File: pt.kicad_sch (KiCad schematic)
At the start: 5 parts, among them J18 PT

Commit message: Updated schematic. No filtering but besides that finished. Need to fix footprints and start layout.
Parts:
- J18: footprint TerminalBlock:TerminalBlock_bornier-3_P5.08mm -> 0UCIRP-KiCAD-Lib:GX-12 3 pin

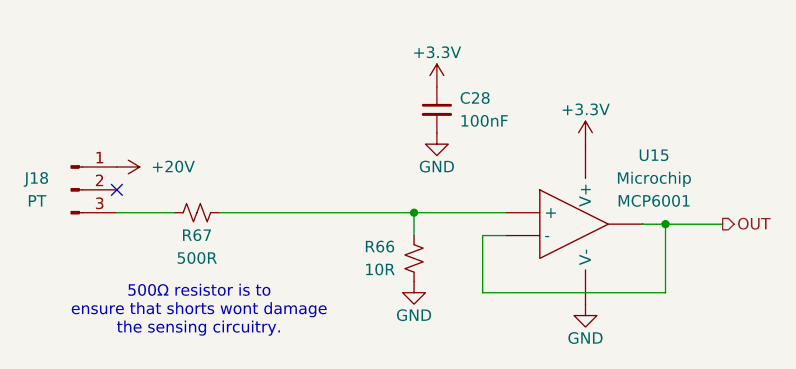
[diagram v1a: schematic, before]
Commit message: Added LC filter for power filtering
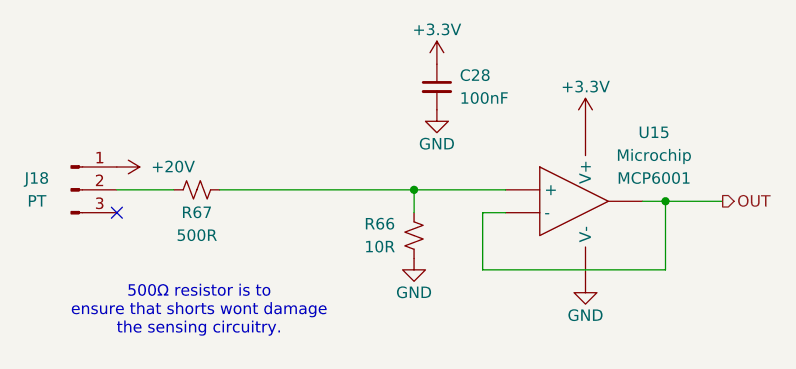
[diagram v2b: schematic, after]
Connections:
- net at J18.2 (Pin_2): now also R67.2
- net at J18.3 (Pin_3): no longer R67.2
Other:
- moved on the sheet: C28, R66, R67, U15

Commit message: Updates after PDR
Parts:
- added C69: ?, Capacitor_SMD:C_0402_1005Metric, symbol Device:C_Small
- added C87: 100nF, Capacitor_SMD:C_0402_1005Metric, symbol Device:C_Small
- added D26: BZT52H, Diode_SMD:D_SOD-123F, symbol UCIRP-KiCAD-Lib:D_Zener_Small
- added R7: 0R, Resistor_SMD:R_0402_1005Metric, symbol Device:R_Small_US
- added U39: ~, Package_TO_SOT_SMD:SOT-23-5, symbol UCIRP-KiCAD-Lib:MCP6001
- R66: value 10R -> 500R
- U15: Manufacturer Microchip -> Texas Instruments; Part # MCP6001 -> LMC7101
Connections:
- net GND: now also C69.2, C87.2, D26.2 (A), U39.2 (V-)
- net OUT: now also U39.1, U39.4 (-); no longer U15.1, U15.4 (-)
- net at R66.2, R67.1, U15.3 (+): now also D26.1 (K)
- net +3.3V renamed +10V
- net +10V: now also C87.1, U39.5 (V+)
- new net: R7.2, U15.1, U15.4 (-)
- new net: C69.1, R7.1, U39.3 (+)
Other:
- note added: "Configurable low pass filter"
- note added: "Zener diode caps voltage at 10V"
- note removed: "500Ω resistor is to ensure that shorts wont damage the sensing circuitry."
- moved on the sheet: R66

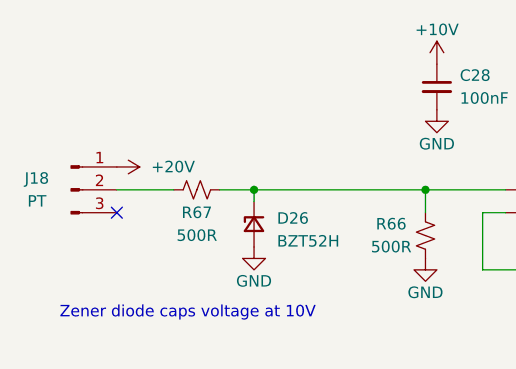
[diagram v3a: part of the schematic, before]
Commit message: Updated to add beginnings of layout. Most major subsystems internally layed out
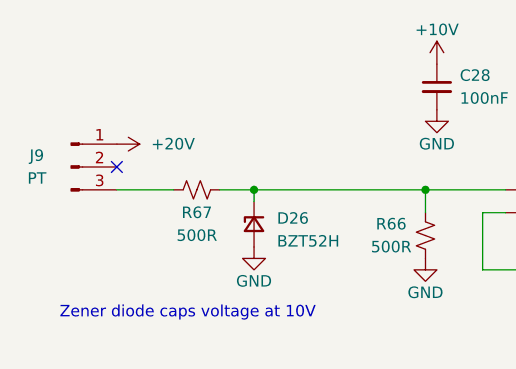
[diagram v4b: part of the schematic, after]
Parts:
- removed J18: PT, 0UCIRP-KiCAD-Lib:GX-12 3 pin, symbol Connector:Conn_01x03_Pin
- added J9: PT, 0UCIRP-KiCAD-Lib:GX-12 3 pin, symbol Connector:Conn_01x03_Pin
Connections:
- net +20V: now also J9.1 (Pin_1)
- net at R67.2: now also J9.3 (Pin_3)
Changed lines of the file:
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@@
 	)
 	(no_connect
-		(at 109.22 96.52)
+		(at 109.22 91.44)
 	)
 	(wire
@@
 	(symbol
 		(lib_id "power:+24V")
-		(at 109.22 91.44 270)
+		(at 109.22 88.9 270)
 		(unit 1)
 		(exclude_from_sim no)
@@
 		(fields_autoplaced yes)
 		(property "Reference" "#PWR0167"
-			(at 105.41 91.44 0)
+			(at 105.41 88.9 0)
 			(effects
 				(font
@@
 		)
 		(property "Value" "+20V"
-			(at 113.03 91.44 90)
+			(at 113.03 88.9 90)
 			(effects
 				(font
@@
 		)
 		(property "Footprint" ""
-			(at 109.22 91.44 0)
+			(at 109.22 88.9 0)
 			(effects
 				(font
@@
 		)
 		(property "Datasheet" ""
-			(at 109.22 91.44 0)
+			(at 109.22 88.9 0)
 			(effects
 				(font
@@
 		)
 		(property "Description" ""
-			(at 109.22 91.44 0)
+			(at 109.22 88.9 0)
 			(effects
 				(font
@@
 	)
 	(symbol
-		(lib_id "Connector:Conn_01x03_Pin")
-		(at 104.14 93.98 0)
-		(unit 1)
-		(exclude_from_sim no)
-		(in_bom yes)
-		(on_board yes)
-		(dnp no)
-		(property "Reference" "J18"
-			(at 100.33 92.71 0)
-			(effects
-				(font
-					(size 1.27 1.27)
-				)
-			)
-		)
-		(property "Value" "PT"
-			(at 100.33 95.25 0)
-			(effects
-				(font
-					(size 1.27 1.27)
-				)
-			)
-		)
-		(property "Footprint" "0UCIRP-KiCAD-Lib:GX-12 3 pin"
-			(at 104.14 93.98 0)
-			(effects
-				(font
-					(size 1.27 1.27)
-				)
-				(hide yes)
-			)
-		)
-		(property "Datasheet" "~"
-			(at 104.14 93.98 0)
-			(effects
-				(font
-					(size 1.27 1.27)
-				)
-				(hide yes)
-			)
-		)
-		(property "Description" ""
-			(at 104.14 93.98 0)
-			(effects
-				(font
-					(size 1.27 1.27)
-				)
-			)
-		)
-		(property "Manufacturer" "~"
-			(at 104.14 93.98 0)
-			(effects
-				(font
-					(size 1.27 1.27)
-				)
-				(hide yes)
-			)
-		)
-		(property "Part #" "~"
-			(at 104.14 93.98 0)
-			(effects
-				(font
-					(size 1.27 1.27)
-				)
-				(hide yes)
-			)
-		)
-		(pin "1"
-		)
-		(pin "2"
-		)
-		(pin "3"
-		)
-		(instances
-			(project "gse2-hardware"
-				(path "/1eb2a3ff-e0fd-4343-8dba-716780a4d459/080ef17d-44b6-48a5-becc-c956f0d3b11f"
-					(reference "J26")
-					(unit 1)
-				)
-				(path "/1eb2a3ff-e0fd-4343-8dba-716780a4d459/0c63aa72-2f8c-4349-a8c7-c0452c52d596"
-					(reference "J18")
-					(unit 1)
-				)
-				(path "/1eb2a3ff-e0fd-4343-8dba-716780a4d459/3a1ca63f-f82f-4b0b-969f-686d8e871d34"
-					(reference "J20")
-					(unit 1)
-				)
-				(path "/1eb2a3ff-e0fd-4343-8dba-716780a4d459/7562866f-379c-4e40-8214-10fa496db888"
-					(reference "J28")
-					(unit 1)
-				)
-				(path "/1eb2a3ff-e0fd-4343-8dba-716780a4d459/90511ce4-e980-4cde-b5eb-16766304f657"
-					(reference "J22")
-					(unit 1)
-				)
-				(path "/1eb2a3ff-e0fd-4343-8dba-716780a4d459/964f4378-b8db-4e43-9e59-375ac742ee34"
-					(reference "J19")
-					(unit 1)
-				)
-				(path "/1eb2a3ff-e0fd-4343-8dba-716780a4d459/b677298a-c5d8-49cc-b7d8-b72cad589e13"
-					(reference "J29")
-					(unit 1)
-				)
-				(path "/1eb2a3ff-e0fd-4343-8dba-716780a4d459/b7b51096-7614-404e-86c5-52fb81f1ca4f"
-					(reference "J24")
-					(unit 1)
-				)
-				(path "/1eb2a3ff-e0fd-4343-8dba-716780a4d459/c5c3a376-27d4-40b8-92ef-c37a3c2b1985"
-					(reference "J25")
-					(unit 1)
-				)
-				(path "/1eb2a3ff-e0fd-4343-8dba-716780a4d459/d31aeae5-8d9f-402f-b6d1-5e5b38396224"
-					(reference "J27")
-					(unit 1)
-				)
-				(path "/1eb2a3ff-e0fd-4343-8dba-716780a4d459/d48db677-5ff5-4889-96a4-25d5500c3d30"
-					(reference "J21")
-					(unit 1)
-				)
-				(path "/1eb2a3ff-e0fd-4343-8dba-716780a4d459/d931e59d-22f9-4efc-a23a-71af672978d6"
-					(reference "J23")
-					(unit 1)
-				)
-			)
-		)
-	)
-	(symbol
 		(lib_id "Device:R_Small_US")
 		(at 143.51 99.06 180)
@@
 					(unit 1)
 				)
+			)
+		)
+	)
+	(symbol
+		(lib_id "Connector:Conn_01x03_Pin")
+		(at 104.14 91.44 0)
+		(unit 1)
+		(exclude_from_sim no)
+		(in_bom yes)
+		(on_board yes)
+		(dnp no)
+		(property "Reference" "J9"
+			(at 100.33 90.17 0)
+			(effects
+				(font
+					(size 1.27 1.27)
+				)
+			)
+		)
+		(property "Value" "PT"
+			(at 100.33 92.71 0)
+			(effects
+				(font
+					(size 1.27 1.27)
+				)
+			)
+		)
+		(property "Footprint" "0UCIRP-KiCAD-Lib:GX-12 3 pin"
+			(at 104.14 91.44 0)
+			(effects
+				(font
+					(size 1.27 1.27)
+				)
+				(hide yes)
+			)
+		)
+		(property "Datasheet" "~"
+			(at 104.14 91.44 0)
+			(effects
+				(font
+					(size 1.27 1.27)
+				)
+				(hide yes)
+			)
+		)
+		(property "Description" ""
+			(at 104.14 91.44 0)
+			(effects
+				(font
+					(size 1.27 1.27)
+				)
+			)
+		)
+		(property "Manufacturer" "~"
+			(at 104.14 91.44 0)
+			(effects
+				(font
+					(size 1.27 1.27)
+				)
+				(hide yes)
+			)
+		)
+		(property "Part #" "~"
+			(at 104.14 91.44 0)
+			(effects
+				(font
+					(size 1.27 1.27)
+				)
+				(hide yes)
+			)
+		)
+		(pin "1"
+		)
+		(pin "2"
+		)
+		(pin "3"
+		)
+		(instances
+			(project "gse2-hardware"
+				(path "/1eb2a3ff-e0fd-4343-8dba-716780a4d459/080ef17d-44b6-48a5-becc-c956f0d3b11f"
+					(reference "J26")
+					(unit 1)
+				)
+				(path "/1eb2a3ff-e0fd-4343-8dba-716780a4d459/0c63aa72-2f8c-4349-a8c7-c0452c52d596"
+					(reference "J9")
+					(unit 1)
+				)
+				(path "/1eb2a3ff-e0fd-4343-8dba-716780a4d459/3a1ca63f-f82f-4b0b-969f-686d8e871d34"
+					(reference "J20")
+					(unit 1)
+				)
+				(path "/1eb2a3ff-e0fd-4343-8dba-716780a4d459/7562866f-379c-4e40-8214-10fa496db888"
+					(reference "J28")
+					(unit 1)
+				)
+				(path "/1eb2a3ff-e0fd-4343-8dba-716780a4d459/90511ce4-e980-4cde-b5eb-16766304f657"
+					(reference "J22")
+					(unit 1)
+				)
+				(path "/1eb2a3ff-e0fd-4343-8dba-716780a4d459/964f4378-b8db-4e43-9e59-375ac742ee34"
+					(reference "J19")
+					(unit 1)
+				)
+				(path "/1eb2a3ff-e0fd-4343-8dba-716780a4d459/b677298a-c5d8-49cc-b7d8-b72cad589e13"
+					(reference "J29")
+					(unit 1)
+				)
+				(path "/1eb2a3ff-e0fd-4343-8dba-716780a4d459/b7b51096-7614-404e-86c5-52fb81f1ca4f"
+					(reference "J24")
+					(unit 1)
+				)
+				(path "/1eb2a3ff-e0fd-4343-8dba-716780a4d459/c5c3a376-27d4-40b8-92ef-c37a3c2b1985"
+					(reference "J25")
+					(unit 1)
+				)
+				(path "/1eb2a3ff-e0fd-4343-8dba-716780a4d459/d31aeae5-8d9f-402f-b6d1-5e5b38396224"
+					(reference "J27")
+					(unit 1)
+				)
+				(path "/1eb2a3ff-e0fd-4343-8dba-716780a4d459/d48db677-5ff5-4889-96a4-25d5500c3d30"
+					(reference "J21")
+					(unit 1)
+				)
+				(path "/1eb2a3ff-e0fd-4343-8dba-716780a4d459/d931e59d-22f9-4efc-a23a-71af672978d6"
+					(reference "J23")
+					(unit 1)
+				)

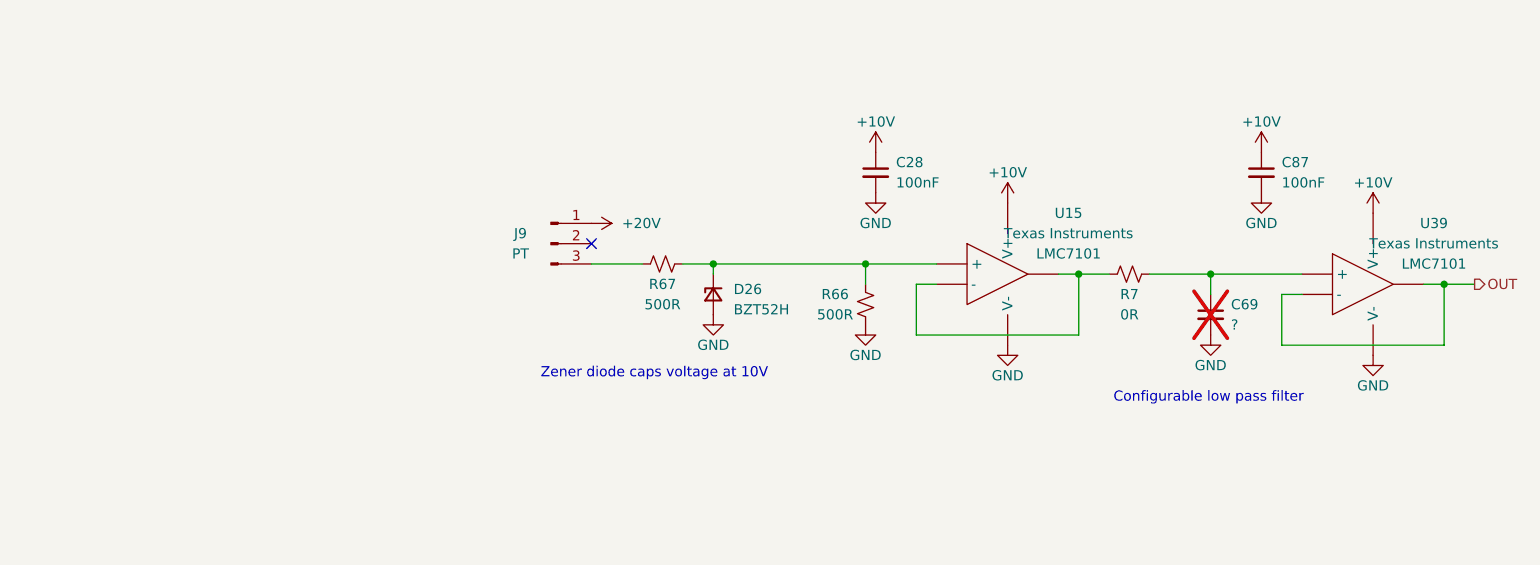
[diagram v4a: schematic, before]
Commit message: Updated to add new filtering circuit
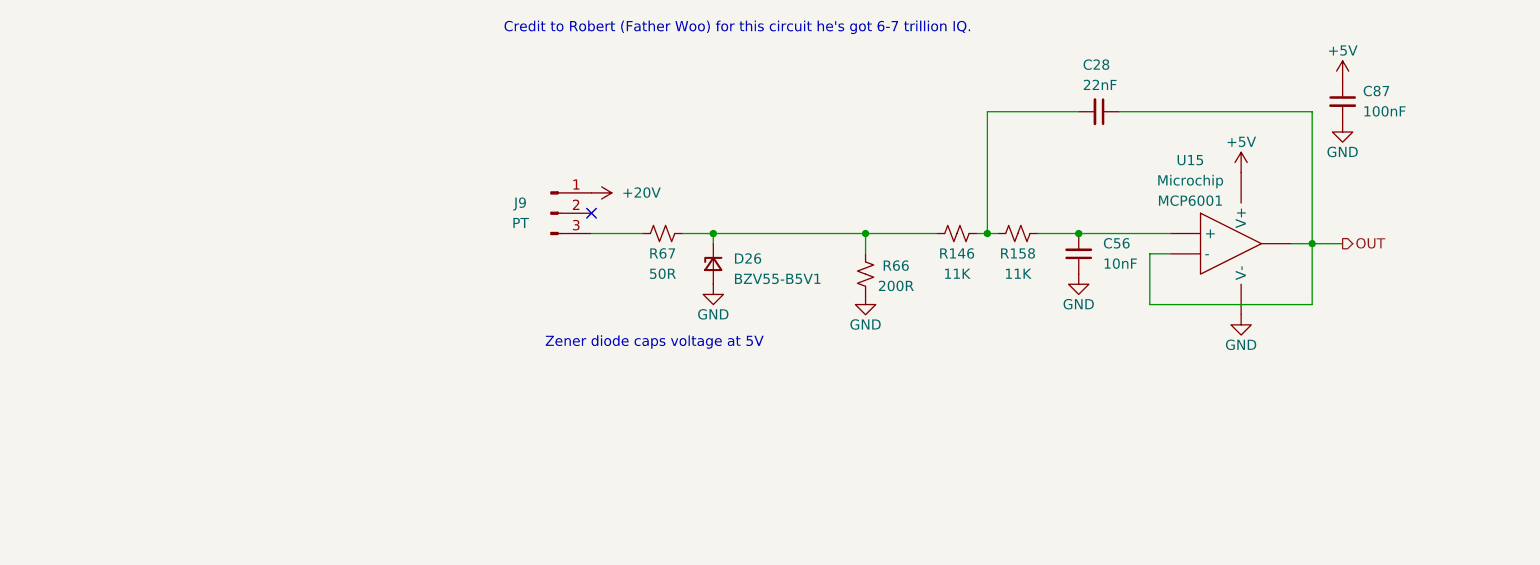
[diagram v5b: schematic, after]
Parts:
- removed C69: ?, Capacitor_SMD:C_0402_1005Metric, symbol Device:C_Small
- removed R7: 0R, Resistor_SMD:R_0402_1005Metric, symbol Device:R_Small_US
- removed U39: ~, Package_TO_SOT_SMD:SOT-23-5, symbol UCIRP-KiCAD-Lib:MCP6001
- added C56: 10nF, Capacitor_SMD:C_0402_1005Metric, symbol Device:C_Small
- added R146, R158: 11K, Resistor_SMD:R_0402_1005Metric, symbol Device:R_Small_US
- C28: value 100nF -> 22nF
- D26: value BZT52H -> BZV55-B5V1; footprint Diode_SMD:D_SOD-123F -> Diode_SMD:D_MiniMELF; Part # BZT52H-A10-QX -> BZV55-B5V1
- R66: value 500R -> 200R
- R67: value 500R -> 50R; footprint Resistor_SMD:R_0402_1005Metric -> Resistor_SMD:R_0603_1608Metric; Part # Generic 1K 1% 0402 Resistor -> (none)
- U15: Manufacturer Texas Instruments -> Microchip; Part # LMC7101 -> MCP6001
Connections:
- net GND: now also C56.1; no longer C28.2
- net OUT: now also C28.1, U15.1, U15.4 (-)
- net at D26.1 (K), R66.2, R67.1: now also R146.2; no longer U15.3 (+)
- net +10V renamed +5V
- net +5V: no longer C28.1
- new net: C56.2, R158.1, U15.3 (+)
- new net: C28.2, R146.1, R158.2
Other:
- note added: "Credit to Robert (Father Woo) for this circuit he's got 6-7 trillion IQ."
- note added: "Zener diode caps voltage at 5V"
- note removed: "Configurable low pass filter"
- note removed: "Zener diode caps voltage at 10V"
- moved on the sheet: C87, J9, R66, R67

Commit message: Subsystem level layout done (prelim)
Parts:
- C28, C56, C87: footprint Capacitor_SMD:C_0402_1005Metric -> Capacitor_SMD:C_0603_1608Metric
- R146, R158, R66: footprint Resistor_SMD:R_0402_1005Metric -> Resistor_SMD:R_0603_1608Metric
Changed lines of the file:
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@@
 			)
 		)
-		(property "Footprint" "Capacitor_SMD:C_0402_1005Metric"
+		(property "Footprint" "Capacitor_SMD:C_0603_1608Metric"
 			(at 170.18 92.71 0)
 			(effects
@@
 			)
 		)
-		(property "Footprint" "Capacitor_SMD:C_0402_1005Metric"
+		(property "Footprint" "Capacitor_SMD:C_0603_1608Metric"
 			(at 172.72 74.93 0)
 			(effects
@@
 			)
 		)
-		(property "Footprint" "Resistor_SMD:R_0402_1005Metric"
+		(property "Footprint" "Resistor_SMD:R_0603_1608Metric"
 			(at 143.51 95.25 0)
 			(effects
@@
 			)
 		)
-		(property "Footprint" "Resistor_SMD:R_0402_1005Metric"
+		(property "Footprint" "Resistor_SMD:R_0603_1608Metric"
 			(at 162.56 90.17 0)
 			(effects
@@
 			)
 		)
-		(property "Footprint" "Capacitor_SMD:C_0402_1005Metric"
+		(property "Footprint" "Capacitor_SMD:C_0603_1608Metric"
 			(at 203.2 73.66 0)
 			(effects
@@
 			)
 		)
-		(property "Footprint" "Resistor_SMD:R_0402_1005Metric"
+		(property "Footprint" "Resistor_SMD:R_0603_1608Metric"
 			(at 154.94 90.17 0)
 			(effects

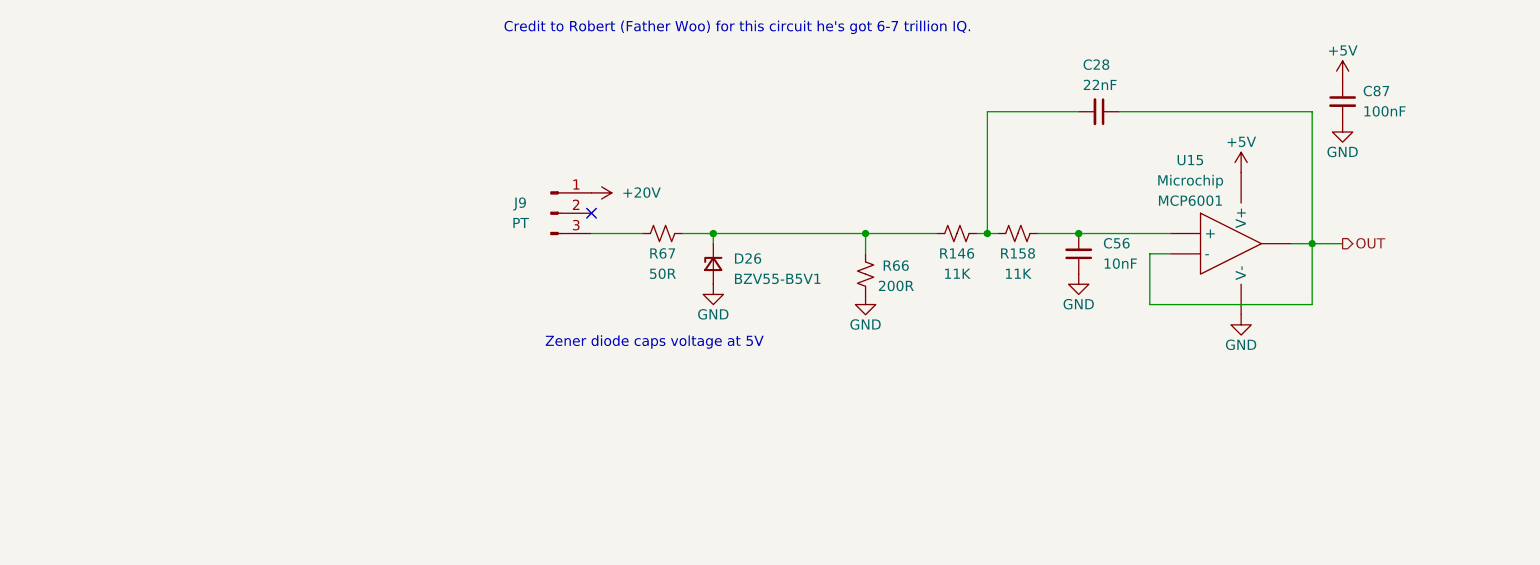
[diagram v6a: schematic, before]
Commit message: Fixed 4-20 ma to support 0-5v
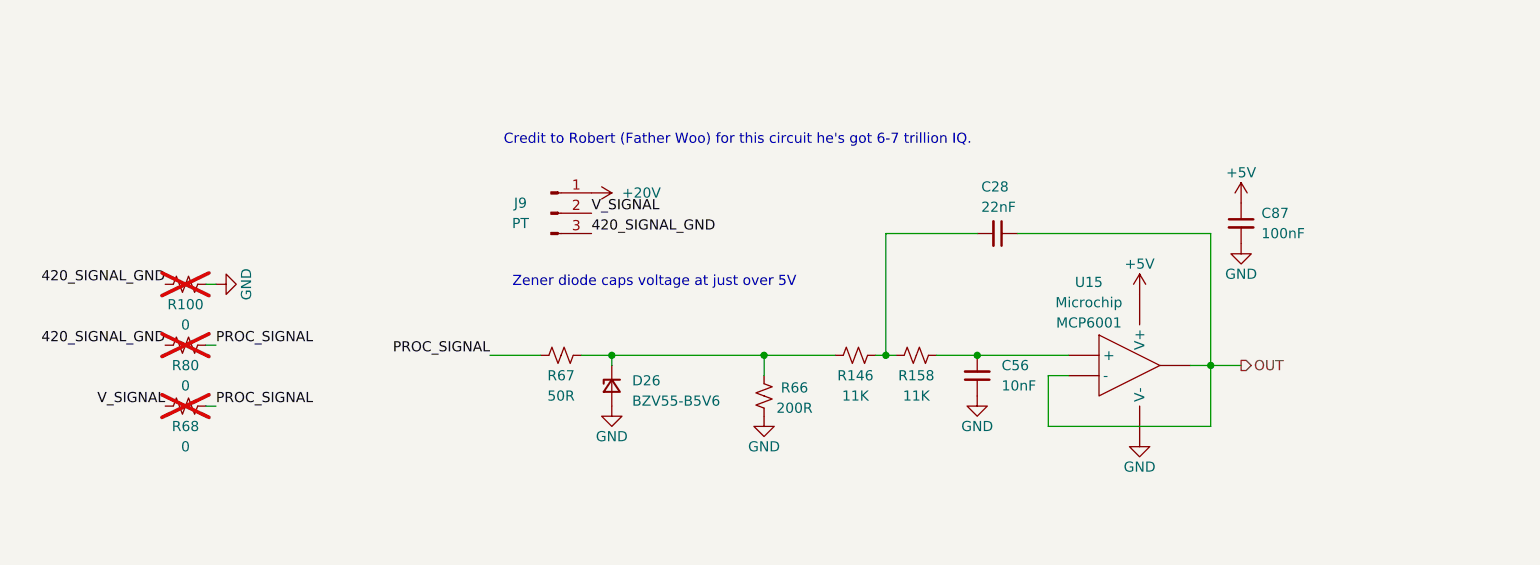
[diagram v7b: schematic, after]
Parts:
- added R100, R68, R80: 0, Resistor_SMD:R_1210_3225Metric_Pad1.30x2.65mm_HandSolder, symbol Device:R_Small_US
- D26: value BZV55-B5V1 -> BZV55-B5V6; Part # BZV55-B5V1 -> BZV55-B5V6
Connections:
- net GND: now also R100.1
- net 420_SIGNAL_GND: now reaches J9.3 (Pin_3)
- net 420_SIGNAL_GND: now also R100.2, R80.2; no longer R67.2
- net V_SIGNAL: now reaches J9.2 (Pin_2)
- net V_SIGNAL: now also R68.2
- new net PROC_SIGNAL: R67.2, R68.1, R80.1
- no-connect marks 1 -> 0
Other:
- note added: "Zener diode caps voltage at just over 5V"
- note removed: "Zener diode caps voltage at 5V"
- moved on the sheet: C28, C56, C87, D26, R146, R158, R66, R67, U15
